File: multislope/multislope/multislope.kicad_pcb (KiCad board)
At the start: 2 copper layers, 91.5 x 49.5 mm, 26 parts, among them P1 CONN_1, P2 CONN_1, P3 CONN_1, P4 CONN_1, P5 CONN_7, P6 CONN_1, U1 A9_REFERENCE, U2 ad711, U3 DG411, U4 ad711, U5 ad711, U6 ad711, U7 ad711

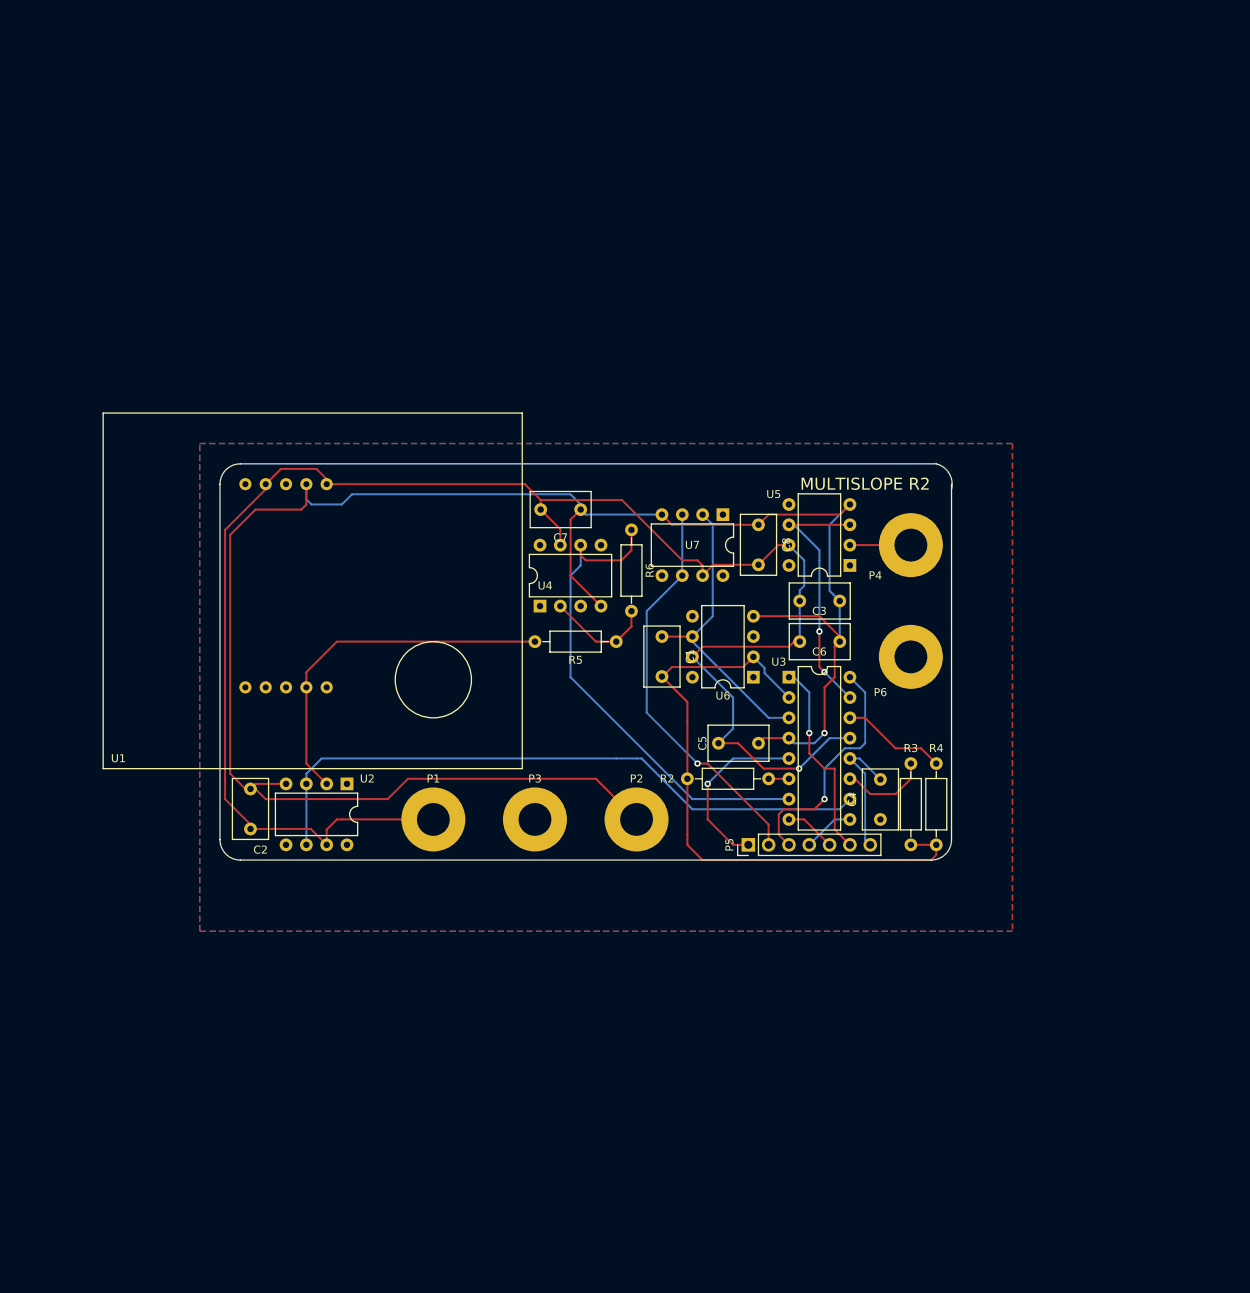
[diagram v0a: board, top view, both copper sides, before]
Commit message: Trying FETs, two opamps in integrator
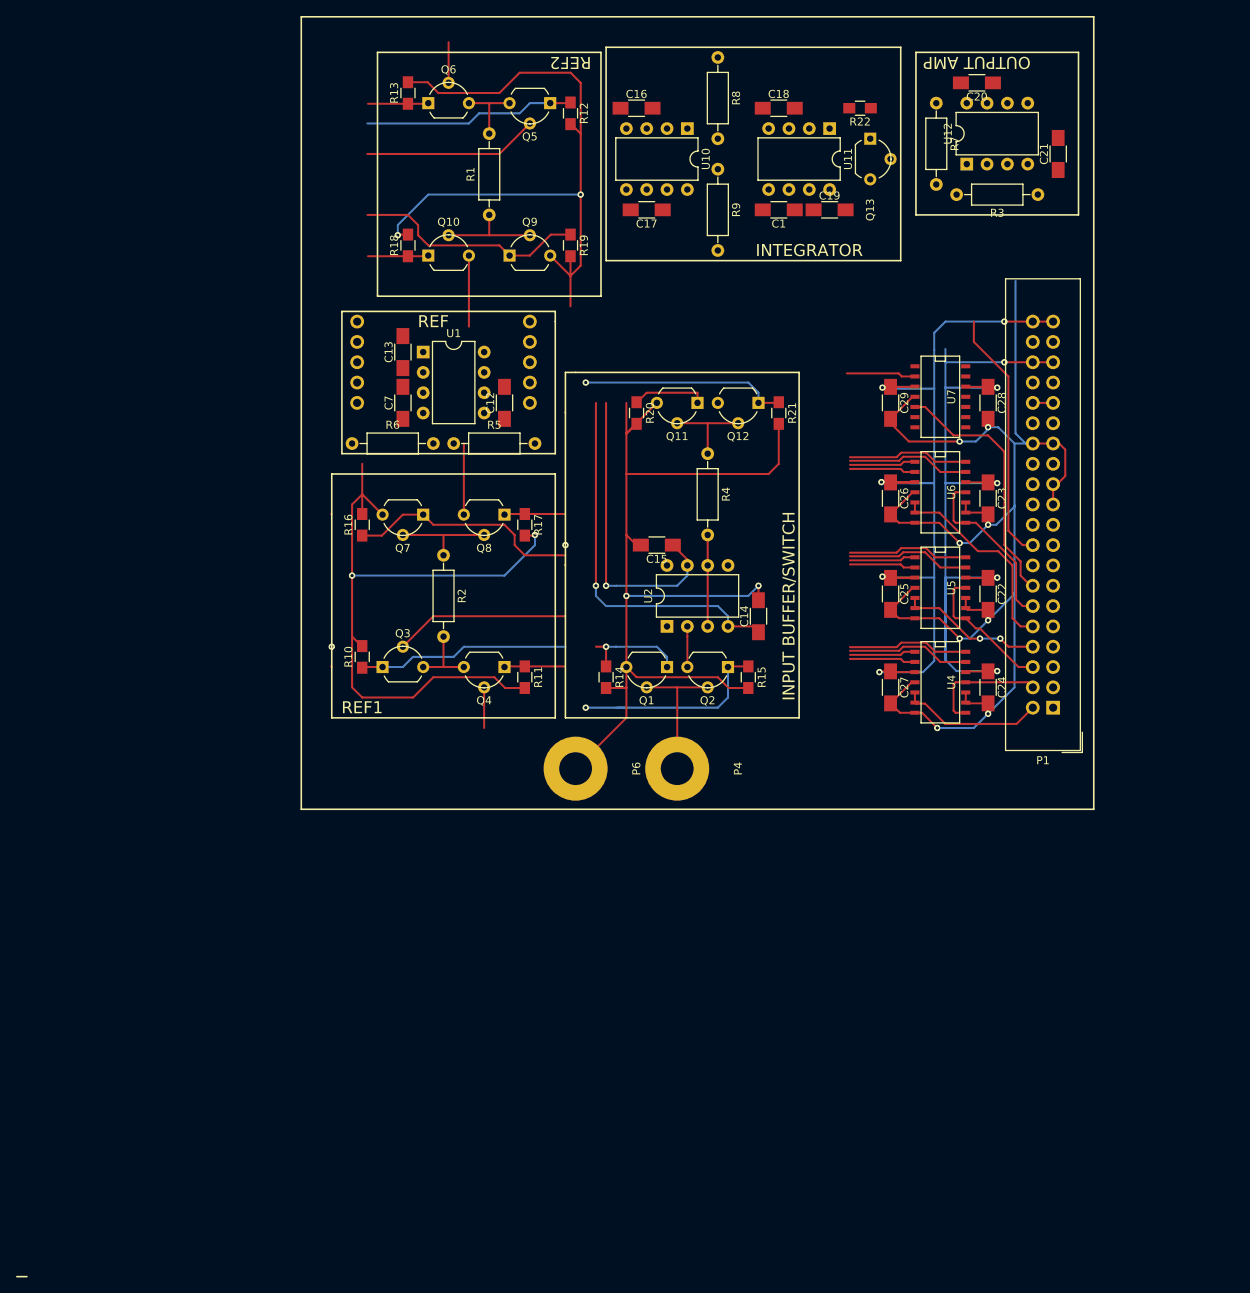
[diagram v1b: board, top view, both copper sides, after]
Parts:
- removed C2, C3, C4, C5, C6, C8: C, Capacitors_THT:C_Disc_D7.5mm_W4.4mm_P5.00mm
- removed P2, P3: CONN_1, 4mm_banana:4mm_banana
- removed P5: CONN_7, Socket_Strips:Socket_Strip_Straight_1x07_Pitch2.54mm
- removed U3: DG411, Housings_DIP:DIP-16_W7.62mm
- added C12: 0.1uF, Capacitors_SMD:C_1206_HandSoldering, F.Cu at (139.7, 81.3)
- added C13: 0.1uF, Capacitors_SMD:C_1206_HandSoldering, F.Cu at (127.0, 74.9)
- added C14: 0.1uF, Capacitors_SMD:C_1206_HandSoldering, F.Cu at (171.4, 108.0)
- added C15: 0.1uF, Capacitors_SMD:C_1206_HandSoldering, F.Cu at (158.8, 99.1)
- added C16: 0.1uF, Capacitors_SMD:C_1206_HandSoldering, F.Cu at (156.2, 44.5)
- added C17: 0.1uF, Capacitors_SMD:C_1206_HandSoldering, F.Cu at (157.5, 57.1)
- added C18: 0.1uF, Capacitors_SMD:C_1206_HandSoldering, F.Cu at (174.0, 44.5)
- added C19: 0.1uF, Capacitors_SMD:C_1206_HandSoldering, F.Cu at (180.3, 57.1)
- added C20: 0.1uF, Capacitors_SMD:C_1206_HandSoldering, F.Cu at (198.8, 41.3)
- added C21: 0.1uF, Capacitors_SMD:C_1206_HandSoldering, F.Cu at (208.9, 50.2)
- added C22: 0.1uF, Capacitors_SMD:C_1206_HandSoldering, F.Cu at (200.2, 105.2)
- added C23: 0.1uF, Capacitors_SMD:C_1206_HandSoldering, F.Cu at (200.2, 93.2)
- added C24: 0.1uF, Capacitors_SMD:C_1206_HandSoldering, F.Cu at (200.2, 116.8)
- added C25: 0.1uF, Capacitors_SMD:C_1206_HandSoldering, F.Cu at (188.0, 105.2)
- added C26: 0.1uF, Capacitors_SMD:C_1206_HandSoldering, F.Cu at (188.0, 93.2)
- added C27: 0.1uF, Capacitors_SMD:C_1206_HandSoldering, F.Cu at (188.0, 116.8)
- added C28: 0.1uF, Capacitors_SMD:C_1206_HandSoldering, F.Cu at (200.2, 81.3)
- added C29: 0.1uF, Capacitors_SMD:C_1206_HandSoldering, F.Cu at (188.0, 81.3)
- added Q1: BF245A, TO_SOT_Packages_THT:TO-92_Molded_Wide, F.Cu at (160.0, 114.3)
- added Q10: BF245A, TO_SOT_Packages_THT:TO-92_Molded_Wide, F.Cu at (130.2, 62.9)
- added Q11: BF245A, TO_SOT_Packages_THT:TO-92_Molded_Wide, F.Cu at (163.8, 81.3)
- added Q12: BF245A, TO_SOT_Packages_THT:TO-92_Molded_Wide, F.Cu at (171.4, 81.3)
- added Q13: BF245A, TO_SOT_Packages_THT:TO-92_Molded_Wide, F.Cu at (185.4, 48.3)
- added Q2: BF245A, TO_SOT_Packages_THT:TO-92_Molded_Wide, F.Cu at (167.6, 114.3)
- added Q3: BF245A, TO_SOT_Packages_THT:TO-92_Molded_Wide, F.Cu at (124.5, 114.3)
- added Q4: BF245A, TO_SOT_Packages_THT:TO-92_Molded_Wide, F.Cu at (139.7, 114.3)
- added Q5: BF245A, TO_SOT_Packages_THT:TO-92_Molded_Wide, F.Cu at (145.4, 43.8)
- added Q6: BF245A, TO_SOT_Packages_THT:TO-92_Molded_Wide, F.Cu at (130.2, 43.8)
- added Q7: BF245A, TO_SOT_Packages_THT:TO-92_Molded_Wide, F.Cu at (129.5, 95.2)
- added Q8: BF245A, TO_SOT_Packages_THT:TO-92_Molded_Wide, F.Cu at (139.7, 95.2)
- added Q9: BF245A, TO_SOT_Packages_THT:TO-92_Molded_Wide, F.Cu at (140.3, 62.9)
- added R1: 6.23M, Resistors_THT:R_Axial_DIN0207_L6.3mm_D2.5mm_P10.16mm_Horizontal, F.Cu at (137.8, 57.8)
- added R10: R, Resistors_SMD:R_0805_HandSoldering, F.Cu at (121.9, 113.0)
- added R11: R, Resistors_SMD:R_0805_HandSoldering, F.Cu at (142.2, 115.6)
- added R12: R, Resistors_SMD:R_0805_HandSoldering, F.Cu at (148.0, 45.1)
- added R13: R, Resistors_SMD:R_0805_HandSoldering, F.Cu at (127.6, 42.5)
- added R14: R, Resistors_SMD:R_0805_HandSoldering, F.Cu at (152.4, 115.6)
- added R15: R, Resistors_SMD:R_0805_HandSoldering, F.Cu at (170.2, 115.6)
- added R16: R, Resistors_SMD:R_0805_HandSoldering, F.Cu at (121.9, 96.5)
- added R17: R, Resistors_SMD:R_0805_HandSoldering, F.Cu at (142.2, 96.5)
- added R18: R, Resistors_SMD:R_0805_HandSoldering, F.Cu at (127.6, 61.6)
- added R19: R, Resistors_SMD:R_0805_HandSoldering, F.Cu at (148.0, 61.6)
- added R20: R, Resistors_SMD:R_0805_HandSoldering, F.Cu at (156.2, 82.5)
- added R21: R, Resistors_SMD:R_0805_HandSoldering, F.Cu at (174.0, 82.5)
- added R22: R, Resistors_SMD:R_0805_HandSoldering, F.Cu at (184.2, 44.5)
- added R7: R, Resistors_THT:R_Axial_DIN0207_L6.3mm_D2.5mm_P10.16mm_Horizontal, F.Cu at (193.7, 43.8)
- added R8: R, Resistors_THT:R_Axial_DIN0207_L6.3mm_D2.5mm_P10.16mm_Horizontal, F.Cu at (166.4, 38.1)
- added R9: R, Resistors_THT:R_Axial_DIN0207_L6.3mm_D2.5mm_P10.16mm_Horizontal, F.Cu at (166.4, 52.1)
- added U0: A9_REFERENCE, A9_REFERENCE:A9REFERENCE, B.Cu at (154.9, 53.3)
- added U10: ad711, Housings_DIP:DIP-8_W7.62mm, F.Cu at (162.6, 47.0)
- added U11: ad711, Housings_DIP:DIP-8_W7.62mm, F.Cu at (180.3, 47.0)
- added U12: ad711, Housings_DIP:DIP-8_W7.62mm, F.Cu at (197.5, 51.4)
- C1, C7: footprint Capacitors_THT:C_Disc_D7.5mm_W4.4mm_P5.00mm -> Capacitors_SMD:C_1206_HandSoldering
- P1: value CONN_1 -> CONN_20X2; footprint 4mm_banana:4mm_banana -> Connectors_IDC:IDC-Header_2x20_Pitch2.54mm_Straight
- R2, R4: value R -> 50K
- U1: value A9_REFERENCE -> LT1013; footprint A9_REFERENCE:A9REFERENCE -> Housings_DIP:DIP-8_W7.62mm
- U4, U5, U6, U7: value ad711 -> LM339; footprint Housings_DIP:DIP-8_W7.62mm -> SMD_Packages:SOIC-14_N
- moved R3 82.8 mm to (206.4, 55.2), turned to 180 degrees
- moved P1 78.7 mm to (208.3, 119.4), turned to 180 degrees
- moved U1 65.7 mm to (129.5, 74.9)
- moved R4 56.6 mm to (165.1, 87.6), turned to 270 degrees
- moved C1 55.3 mm to (174.0, 57.1), turned to 180 degrees
- moved U4 51.1 mm to (194.3, 116.2), turned to 270 degrees
- moved U2 44.6 mm to (160.0, 109.2), turned to 90 degrees
- moved P6 44.2 mm to (148.6, 127.0), turned to 90 degrees
- moved R2 41.3 mm to (132.1, 100.3), turned to 270 degrees
- moved P4 40.4 mm to (161.3, 127.0), turned to 90 degrees
- moved R6 36.6 mm to (120.7, 86.4), turned to 0 degrees
- moved U6 33.0 mm to (194.3, 92.5), turned to 270 degrees
- moved R5 32.0 mm to (133.3, 86.4), turned to 0 degrees
- moved U7 31.0 mm to (194.3, 80.5)
- moved C7 25.9 mm to (127.0, 81.3), turned to 90 degrees
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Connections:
- P1 pad 1: +12V -> SCLK
- R2 pad 1: Net-(C1-Pad2) -> Net-(Q7-Pad2)
- R3 pad 1: Net-(C1-Pad2) -> GND
- R4 pad 1: Net-(C1-Pad2) -> Net-(Q11-Pad2)
- U2 pad 2: Net-(R5-Pad2) -> Net-(Q2-Pad3)
- U2 pad 3: REF_PLUS -> Net-(R4-Pad2)
- U2 pad 6: REF_PLUS -> Net-(R4-Pad2)
- U4 pad 1: (no net) -> SW_REF1A_INV
- U4 pad 2: Net-(R5-Pad1) -> SW_REF1A
- U4 pad 3: GND -> +12V
- U4 pad 4: -12V -> GND
- U4 pad 5: (no net) -> SW_REF1A_INTERFACE
- U4 pad 6: REF_MINUS -> SW_REF1A_INTERFACE
- U4 pad 7: +12V -> GND
- U4 pad 8: (no net) -> SW_REF1B_INTERFACE
- U5 pad 1: (no net) -> SW_REF2B_INV
- U5 pad 2: Net-(P4-Pad1) -> SW_REF2B
- U5 pad 3: Net-(U3-Pad15) -> +12V
- U5 pad 4: -12V -> GND
- U5 pad 5: (no net) -> SW_REF2B_INTERFACE
- U5 pad 6: Net-(U3-Pad15) -> SW_REF2B_INTERFACE
- U5 pad 7: +12V -> GND
- U5 pad 8: (no net) -> SW_REF2A_INTERFACE
- U6 pad 1: (no net) -> SW_INPUT1_INV
- U6 pad 2: Net-(C1-Pad2) -> SW_INPUT1
- U6 pad 3: GND -> +12V
- U6 pad 4: -12V -> GND
- U6 pad 5: (no net) -> SW_INPUT1_INTERFACE
- U6 pad 6: Net-(C1-Pad1) -> SW_INPUT1_INTERFACE
- U6 pad 7: +12V -> GND
- U6 pad 8: (no net) -> SW_INPUT2_INTERFACE
- U7 pad 2: Net-(C1-Pad1) -> SW_RST
- U7 pad 3: CMP_OUT -> +12V
- U7 pad 4: -12V -> GND
- U7 pad 5: (no net) -> SW_RST_INTERFACE
- U7 pad 6: CMP_OUT -> (no net)
- U7 pad 7: +12V -> (no net)
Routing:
- net GND: track 22.3 -> 471.0 mm, vias 1 -> 14
- net -12V: track 245.8 -> 152.9 mm, vias 1 -> 6
- net SW_REF1B: track 0.00 -> 74.1 mm
- net REF_PLUS: track 80.8 -> 10.2 mm
- net Net-(C1-Pad2): track 78.3 -> 17.8 mm
- net +12V: track 214.6 -> 156.0 mm, vias 1 -> 6
- net Net-(R5-Pad2): track 45.2 -> 0.00 mm
- net SW_REF2A: track 0.00 -> 42.0 mm, vias 0 -> 1
- net SW_INPUT2_INV: track 0.00 -> 41.1 mm, vias 0 -> 1
- net Net-(C1-Pad1): track 37.3 -> 0.00 mm
- net SW_REF1A: track 0.00 -> 34.8 mm, vias 0 -> 1
- net SW_INPUT1_INV: track 0.00 -> 34.2 mm, vias 0 -> 1
- net Net-(U3-Pad15): track 32.7 -> 0.00 mm, vias 2 -> 0
- net SW_RST_INTERFACE: track 0.00 -> 31.9 mm
- net SW_REF1B_INV: track 0.00 -> 30.6 mm
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- removed copper zone on B.Cu, net GND
- removed copper zone on F.Cu, net GND
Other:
- board outline removed
- board text added: "INPUT BUFFER/SWITCH"
- board text added: "INTEGRATOR"
- board text added: "OUTPUT AMP"
- board text added: "REF"
- board text added: "REF1"
- board text added: "REF2"
- board text removed: "MULTISLOPE R2"

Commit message: current multislope
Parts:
- removed C14, C15, C22, C23, C24, C25, C26, C27, C28, C29: 0.1uF, Capacitors_SMD:C_1206_HandSoldering
- removed Q1, Q10, Q11, Q12, Q13, Q2, Q3, Q4, Q5, Q6, Q7, Q8, Q9: BF245A, TO_SOT_Packages_THT:TO-92_Molded_Wide
- removed R1: 6.23M, Resistors_THT:R_Axial_DIN0207_L6.3mm_D2.5mm_P10.16mm_Horizontal
- removed R10, R11, R12, R13, R14, R15, R16, R17, R18, R19, R20, R21, R22: R, Resistors_SMD:R_0805_HandSoldering
- removed R2, R4: 50K, Resistors_THT:R_Axial_DIN0207_L6.3mm_D2.5mm_P10.16mm_Horizontal
- removed U2: ad711, Housings_DIP:DIP-8_W7.62mm
- removed U4, U5, U6, U7: LM339, SMD_Packages:SOIC-14_N
- added C1000: 10nF, Capacitors_SMD:C_1206_HandSoldering, F.Cu at (150.4, 111.3)
- added C1001: 10nF, Capacitors_SMD:C_1206_HandSoldering, F.Cu at (150.4, 117.9)
- added C1010: 10nF, Capacitors_SMD:C_1206_HandSoldering, F.Cu at (161.9, 111.3)
- added C1011: 10nF, Capacitors_SMD:C_1206_HandSoldering, F.Cu at (161.9, 117.9)
- added C1020: 10nF, Capacitors_SMD:C_1206_HandSoldering, F.Cu at (173.3, 111.3)
- added C1021: 10nF, Capacitors_SMD:C_1206_HandSoldering, F.Cu at (173.3, 117.9)
- added C1030: 10nF, Capacitors_SMD:C_1206_HandSoldering, F.Cu at (184.7, 111.3)
- added C1031: 10nF, Capacitors_SMD:C_1206_HandSoldering, F.Cu at (184.7, 117.9)
- added C2000: 10nF, Capacitors_SMD:C_1206_HandSoldering, F.Cu at (208.3, 106.2)
- added C2001: 10nF, Capacitors_SMD:C_1206_HandSoldering, F.Cu at (214.9, 106.2)
- added C2010: 0.1uF, Capacitors_SMD:C_1206_HandSoldering, F.Cu at (219.2, 95.8)
- added C2011: 0.1uF, Capacitors_SMD:C_1206_HandSoldering, F.Cu at (206.0, 95.2)
- added C2020: 10nF, Capacitors_SMD:C_1206_HandSoldering, F.Cu at (202.2, 84.8)
- added C2021: 10nF, Capacitors_SMD:C_1206_HandSoldering, F.Cu at (198.1, 82.8)
- added C31: 10nF, Capacitors_SMD:C_1206_HandSoldering, F.Cu at (181.1, 83.6)
- added C32: 10nF, Capacitors_SMD:C_1206_HandSoldering, F.Cu at (188.0, 83.6)
- added R100: 50K, Resistors_THT:R_Axial_DIN0207_L6.3mm_D2.5mm_P10.16mm_Horizontal, F.Cu at (157.2, 115.1)
- added R101: 50K, Resistors_THT:R_Axial_DIN0207_L6.3mm_D2.5mm_P10.16mm_Horizontal, F.Cu at (168.7, 115.1)
- added R102: 6.23M, Resistors_THT:R_Axial_DIN0207_L6.3mm_D2.5mm_P10.16mm_Horizontal, F.Cu at (180.1, 115.1)
- added R103: 6.23M, Resistors_THT:R_Axial_DIN0207_L6.3mm_D2.5mm_P10.16mm_Horizontal, F.Cu at (191.5, 115.1)
- added R200: 50K, Resistors_THT:R_Axial_DIN0207_L6.3mm_D2.5mm_P10.16mm_Horizontal, F.Cu at (203.7, 89.2)
- added U100: DG419, Housings_SSOP:MSOP-8_3x3mm_Pitch0.65mm, F.Cu at (153.5, 114.6)
- added U101: DG419, Housings_SSOP:MSOP-8_3x3mm_Pitch0.65mm, F.Cu at (164.9, 114.6)
- added U102: DG419, Housings_SSOP:MSOP-8_3x3mm_Pitch0.65mm, F.Cu at (176.3, 114.6)
- added U103: DG419, Housings_SSOP:MSOP-8_3x3mm_Pitch0.65mm, F.Cu at (187.8, 114.6)
- added U16: DG417, Housings_SSOP:MSOP-8_3x3mm_Pitch0.65mm, F.Cu at (184.9, 86.6)
- added U200: DG419, Housings_SSOP:MSOP-8_3x3mm_Pitch0.65mm, F.Cu at (214.9, 102.9)
- added U201: ad711, Housings_DIP:DIP-8_W7.62mm, F.Cu at (208.8, 99.6)
- added U202: DG419, Housings_SSOP:MSOP-8_3x3mm_Pitch0.65mm, F.Cu at (199.0, 88.0)
- P4: value CONN_1 -> +
- P6: value CONN_1 -> GND
- U0: moved to F.Cu
- moved R6 102.3 mm to (215.1, 125.5), turned to 90 degrees
- moved C7 95.5 mm to (209.8, 128.8), turned to 180 degrees
- moved C13 93.1 mm to (202.9, 128.8), turned to 180 degrees
- moved U1 90.6 mm to (204.2, 126.2), turned to 90 degrees
- moved C12 89.5 mm to (214.1, 131.1), turned to 0 degrees
- moved P6 84.7 mm to (224.5, 89.4), turned to 180 degrees
- moved R5 83.7 mm to (211.8, 115.3), turned to 180 degrees
- moved P1 83.0 mm to (135.9, 78.7), turned to 0 degrees
- moved C20 73.5 mm to (144.8, 91.2), turned to 90 degrees
- moved R7 73.1 mm to (145.8, 99.1), turned to 0 degrees
- moved P4 68.0 mm to (224.5, 102.1), turned to 180 degrees
- moved C21 66.1 mm to (152.9, 85.3), turned to 180 degrees
- moved U12 61.4 mm to (154.9, 95.8), turned to 180 degrees
- moved C18 59.4 mm to (183.4, 103.1)
- moved R3 55.8 mm to (158.0, 83.1), turned to 270 degrees
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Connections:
- net Net-(P1-Pad31) renamed +5V
- P1 pad 10: SW_INPUT1_INTERFACE -> SW_REF2B
- P1 pad 12: SW_INPUT2_INTERFACE -> SW_REF2A
- P1 pad 14: SW_RST_INTERFACE -> SW_REF1B
- P1 pad 16: Net-(P1-Pad16) -> SW_REF1A
- P1 pad 2: SW_REF1A_INTERFACE -> SW_RST
- P1 pad 4: SW_REF1B_INTERFACE -> Net-(P1-Pad4)
- P1 pad 6: SW_REF2A_INTERFACE -> SW_INPUT2
- P1 pad 8: SW_REF2B_INTERFACE -> SW_INPUT1
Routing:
- net -12V: track 152.9 -> 948.4 mm, vias 6 -> 27
- net GND: track 471.0 -> 1168.4 mm, vias 14 -> 40
- net +5V: track 2.54 -> 207.4 mm, vias 0 -> 10
- net Net-(C1-Pad2): track 17.8 -> 167.5 mm, vias 0 -> 2
- net +12V: track 156.0 -> 283.4 mm, vias 6 -> 9
- net SW_INPUT1: track 21.4 -> 118.3 mm
- net SW_REF2B: track 8.29 -> 94.6 mm, vias 0 -> 2
- net Net-(C1-Pad1): track 0.00 -> 50.9 mm, vias 0 -> 1
- net SW_RST: track 8.67 -> 58.8 mm, vias 0 -> 1
- net SW_INPUT2: track 24.9 -> 69.4 mm, vias 0 -> 2
- net REF_PLUS: track 10.2 -> 54.1 mm, vias 0 -> 1
- net SW_INPUT2_INV: track 41.1 -> 0.00 mm, vias 1 -> 0
- net REF_MINUS: track 43.8 -> 84.5 mm
- net SW_REF2A: track 42.0 -> 80.1 mm, vias 1 -> 2
- net SW_INPUT1_INV: track 34.2 -> 0.00 mm, vias 1 -> 0
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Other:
- board outline added: 99.1 x 64.8 mm
- board text added: "INPUT"
- board text added: "Large"
- board text added: "MULTISLOPE R1"
- board text added: "REF SLOPE"
- board text added: "Small"
- board text removed: "INPUT BUFFER/SWITCH"
- board text removed: "REF"
- board text removed: "REF1"
- board text removed: "REF2"
